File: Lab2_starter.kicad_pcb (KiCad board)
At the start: 4 copper layers, 123.2 x 64.6 mm, 78 parts, among them J1 973582101, J10 Conn_01x02, J11 Conn_01x02, J12 Conn_01x02, J13 Conn_01x02, J14 Conn_01x02, J15 Conn_01x02, J16 Conn_01x02, J2 973582100, J3 973582101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

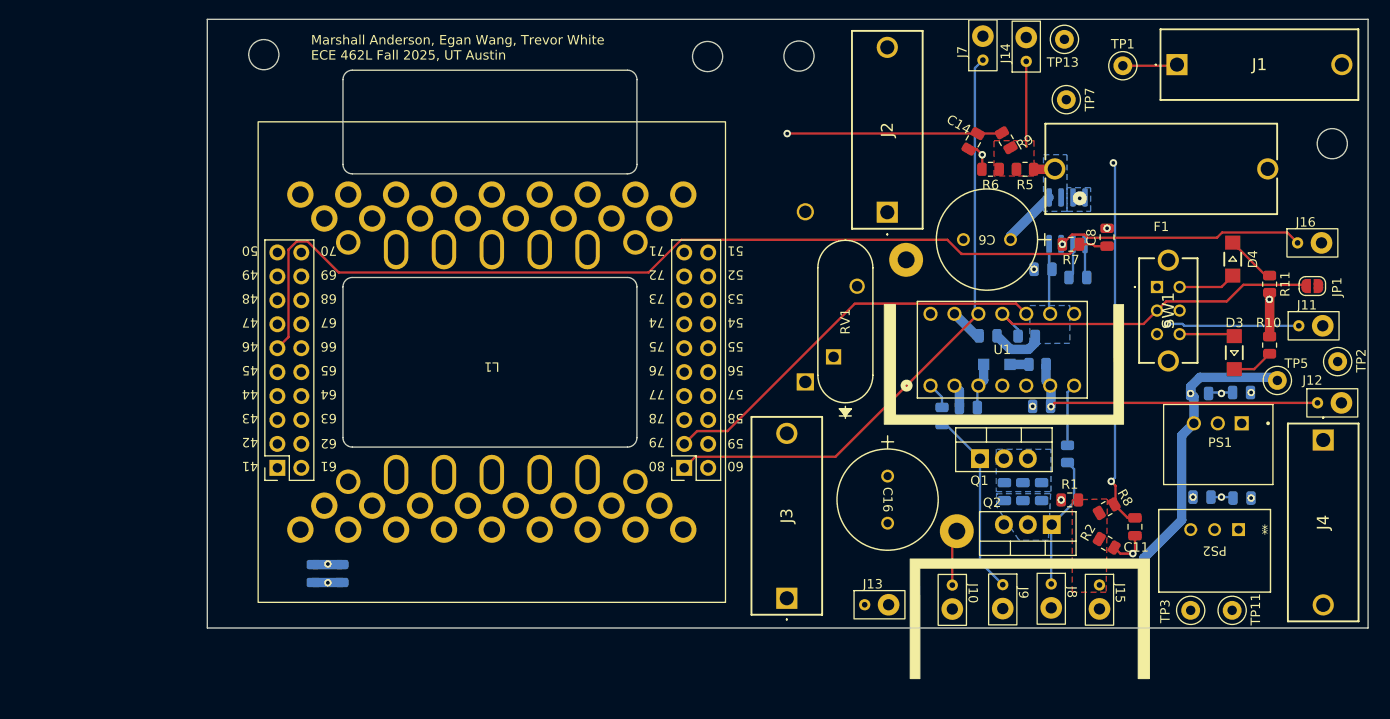
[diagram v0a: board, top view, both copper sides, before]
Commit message: Moved decoupling RC filters next to C2000 IO pins
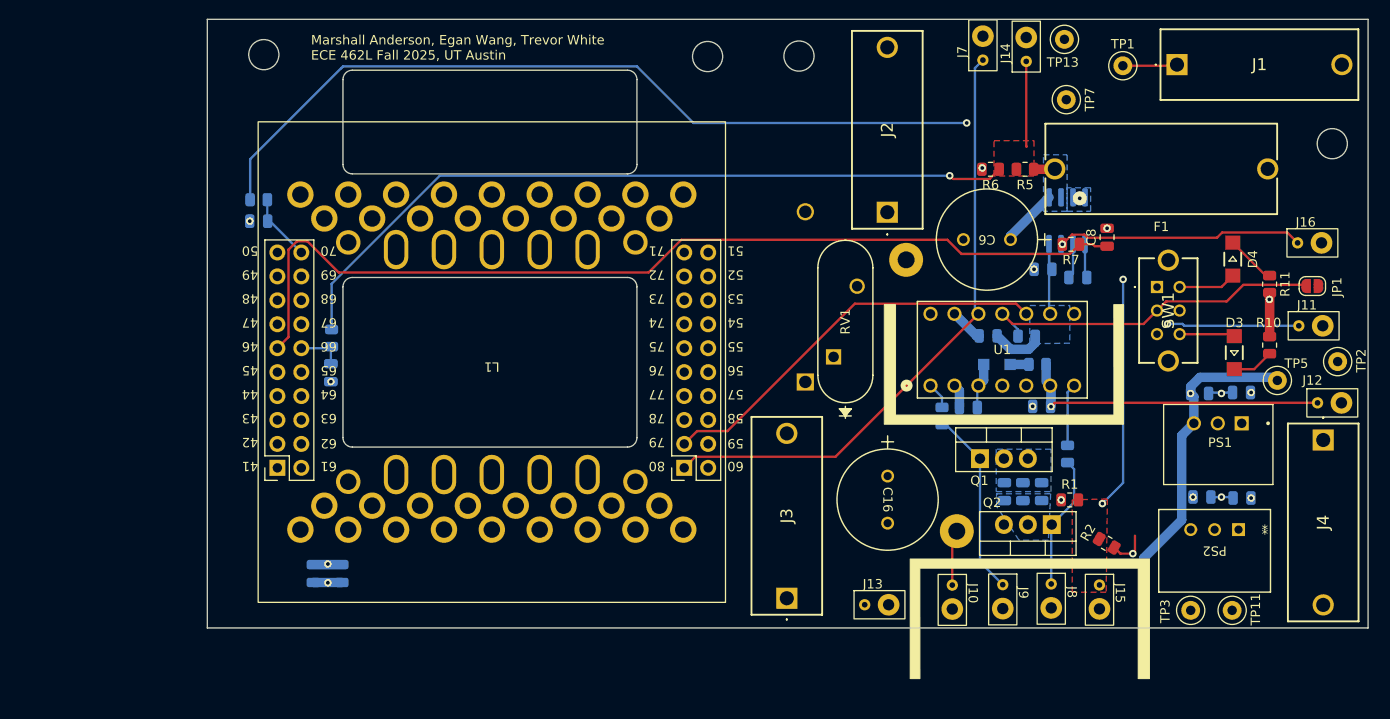
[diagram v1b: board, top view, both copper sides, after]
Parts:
- C11, C14, R8, R9: moved to B.Cu
- moved C11 98.5 mm to (36.5, 54.8), turned to 180 degrees
- moved R8 95.8 mm to (36.5, 52.5), turned to 180 degrees
- moved R9 74.6 mm to (44.2, 67.2), turned to 90 degrees
- moved C14 72.5 mm to (44.1, 70.9), turned to -90 degrees
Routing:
- net /ADCINA0: track 150.8 -> 7.24 mm, vias 2 -> 0
- net Vout_sens: track 0.00 -> 139.1 mm, vias 0 -> 3
- net Vin_sens: track 9.08 -> 90.1 mm, vias 0 -> 1
- net /ADCINA4: track 85.9 -> 5.12 mm, vias 1 -> 0
- net GND: track 26.6 -> 23.4 mm, vias 8 -> 10

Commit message: Add files via upload
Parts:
- C12, C15, C9: moved to F.Cu
- moved C15 3.95 mm to (115.6, 83.5)
- moved C9 3.95 mm to (119.5, 83.5)
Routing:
- added copper zone on F.Cu, net GND
- added copper zone on F.Cu, net Vout
- removed copper zone on B.Cu, net GND
- removed copper zone on B.Cu, net Vout

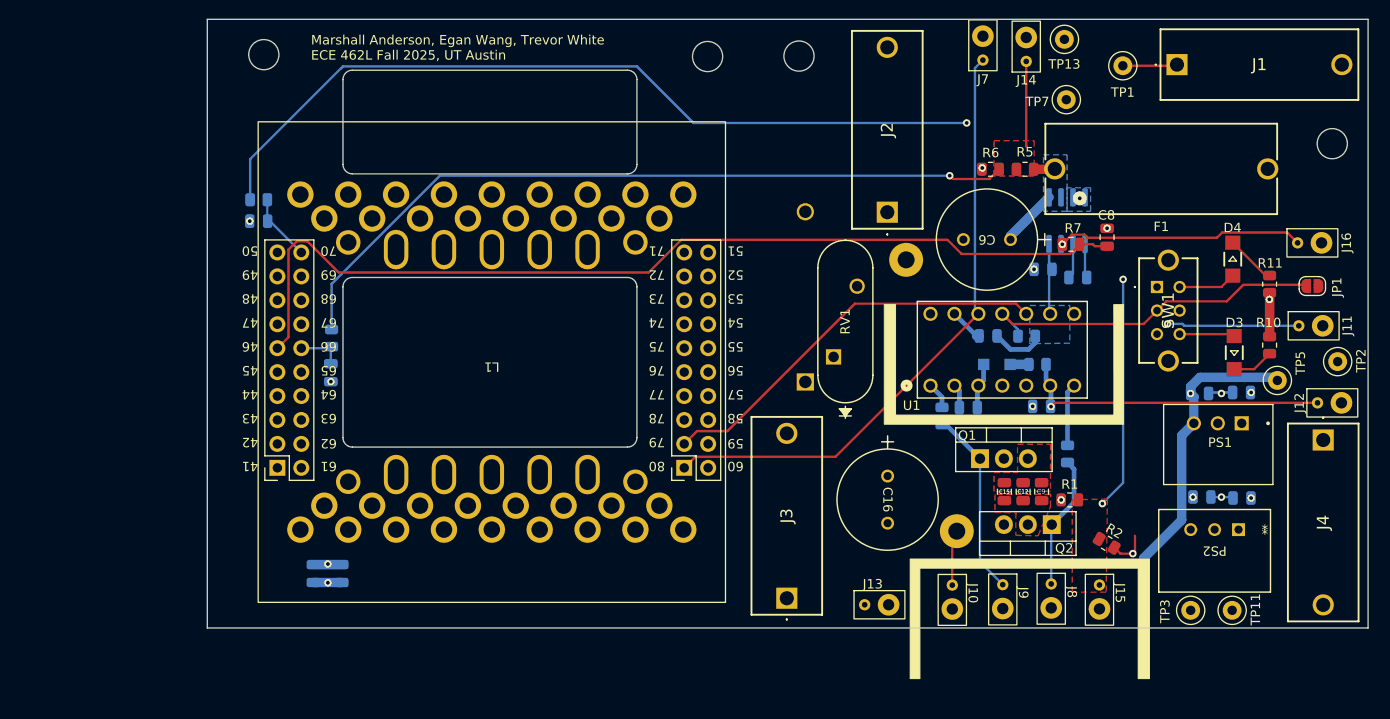
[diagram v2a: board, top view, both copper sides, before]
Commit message: updated PCB annulus, changed ADC traces
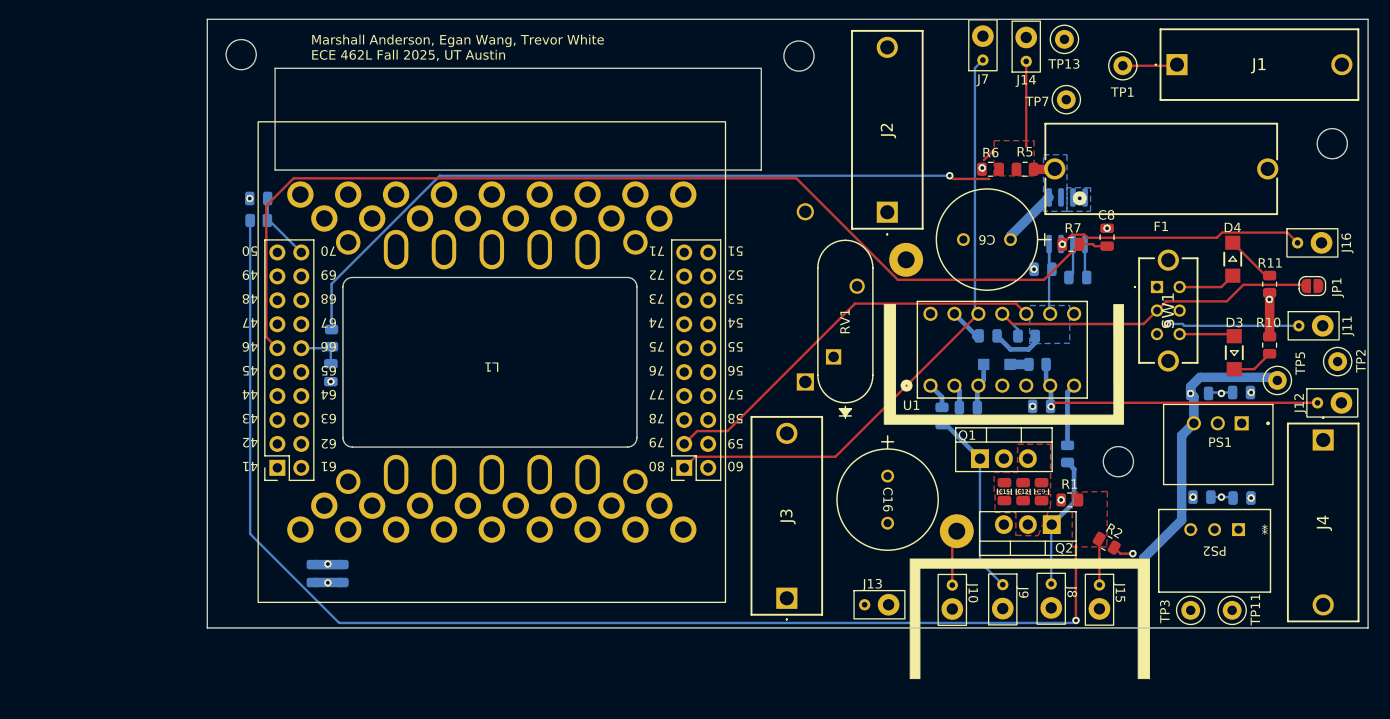
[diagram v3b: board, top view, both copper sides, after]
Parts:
- moved H4 61.2 mm to (127.7, 80.3)
- moved C11 2.40 mm to (36.5, 52.4)
- moved H3 2.40 mm to (34.6, 37.1)
- moved R8 2.20 mm to (36.5, 54.7)
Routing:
- net /ADCINA9: track 102.2 -> 112.2 mm
- net GND: track 23.4 -> 21.4 mm
- net Vout_sens: track 139.1 -> 137.8 mm, vias 3 -> 1
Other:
- outline, holes or cut-outs redrawn
- board text added: "{dblquote}High di/dt paths are inevitable in class society.{dblquote} -Mao Zedong"

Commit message: edited Mao quote spacing, further reduced board size
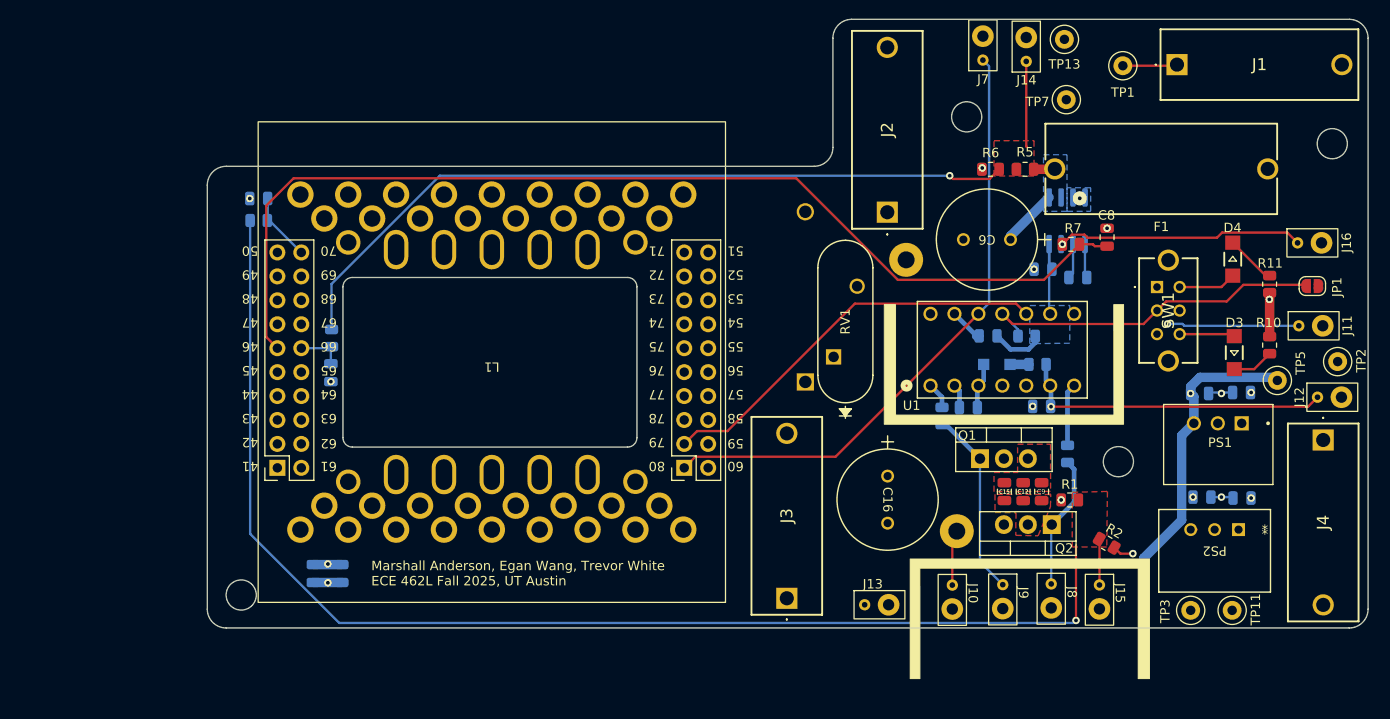
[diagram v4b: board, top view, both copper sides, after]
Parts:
- moved H1 82.3 mm to (34.6, 94.5)
- moved H3 77.3 mm to (111.6, 43.8)
- moved J12 0.60 mm to (150.1, 73.5)
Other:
- outline, holes or cut-outs redrawn
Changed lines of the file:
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@@
 	(footprint "MountingHole:MountingHole_3.2mm_M3"
 		(layer "F.Cu")
-		(at 93.8 37.3)
+		(at 34.6 94.5)
 		(descr "Mounting Hole 3.2mm, no annular, M3")
 		(tags "mounting hole 3.2mm no annular m3")
@@
 	(footprint "MountingHole:MountingHole_3.2mm_M3"
 		(layer "F.Cu")
-		(at 34.6 37.15)
+		(at 111.6 43.75)
 		(descr "Mounting Hole 3.2mm, no annular, M3")
 		(tags "mounting hole 3.2mm no annular m3")
@@
 	(footprint "ECE462L:TP"
 		(layer "F.Cu")
-		(at 150.105 74.108183)
+		(at 150.105 73.508183)
 		(property "Reference" "J12"
 			(at -3.185 0.001817 90)
@@
 		(layer "Edge.Cuts")
 	)
-	(gr_rect
-		(start 38.2 38.6)
-		(end 89.8 49.4)
+	(gr_line
+		(start 97.4 47)
+		(end 97.4 35.4)
 		(stroke
 			(width 0.1)
 			(type default)
 		)
-		(fill no)
 		(layer "Edge.Cuts")
 	)
-	(gr_rect
-		(start 31 33.4)
-		(end 154.2 98)
+	(gr_arc
+		(start 97.4 47)
+		(mid 96.814214 48.414214)
+		(end 95.4 49)
+		(stroke
+			(width 0.1)
+			(type default)
+		)
+		(layer "Edge.Cuts")
+	)
+	(gr_line
+		(start 152.2 98)
+		(end 33 98)
+		(stroke
+			(width 0.1)
+			(type default)
+		)
+		(layer "Edge.Cuts")
+	)
+	(gr_arc
+		(start 152.2 33.4)
+		(mid 153.614214 33.985786)
+		(end 154.2 35.4)
+		(stroke
+			(width 0.1)
+			(type default)
+		)
+		(layer "Edge.Cuts")
+	)
+	(gr_arc
+		(start 33 98)
+		(mid 31.585786 97.414214)
+		(end 31 96)
 		(stroke
 			(width 0.1)
 			(type default)
 		)
-		(fill no)
 		(layer "Edge.Cuts")
 	)
@@
 		(layer "Edge.Cuts")
 	)
+	(gr_arc
+		(start 31 51)
+		(mid 31.585786 49.585786)
+		(end 33 49)
+		(stroke
+			(width 0.1)
+			(type default)
+		)
+		(layer "Edge.Cuts")
+	)
+	(gr_arc
+		(start 97.4 35.4)
+		(mid 97.985786 33.985786)
+		(end 99.4 33.4)
+		(stroke
+			(width 0.1)
+			(type default)
+		)
+		(layer "Edge.Cuts")
+	)
+	(gr_line
+		(start 95.4 49)
+		(end 33 49)
+		(stroke
+			(width 0.1)
+			(type default)
+		)
+		(layer "Edge.Cuts")
+	)
+	(gr_line
+		(start 31 96)
+		(end 31 51)
+		(stroke
+			(width 0.1)
+			(type default)
+		)
+		(layer "Edge.Cuts")
+	)
+	(gr_arc
+		(start 154.2 96)
+		(mid 153.614214 97.414214)
+		(end 152.2 98)
+		(stroke
+			(width 0.1)
+			(type default)
+		)
+		(layer "Edge.Cuts")
+	)
 	(gr_line
 		(start 75.6 78.8)
@@
 	)
 	(gr_line
+		(start 99.4 33.4)
+		(end 152.2 33.4)
+		(stroke
+			(width 0.1)
+			(type default)
+		)
+		(layer "Edge.Cuts")
+	)
+	(gr_line
 		(start 76.6 61.8)
 		(end 76.6 77.8)
@@
 		(layer "Edge.Cuts")
 	)
+	(gr_line
+		(start 154.2 35.4)
+		(end 154.2 96)
+		(stroke
+			(width 0.1)
+			(type default)
+		)
+		(layer "Edge.Cuts")
+	)
 	(gr_rect
 		(start 30.95 33.4)
@@
 	)
 	(gr_text "Marshall Anderson, Egan Wang, Trevor White\nECE 462L Fall 2025, UT Austin"
-		(at 42 37.8 0)
+		(at 48.4 93.6 0)
 		(layer "F.SilkS")
 		(effects
@@
 		)
 	)
-	(gr_text "{dblquote}High di/dt paths are \ninevitable in class \nsociety.{dblquote} -Mao Zedong"
-		(at 108.151445 48.392694 0)
+	(gr_text "{dblquote}High di/dt \npaths are \ninevitable \nin class \nsociety.{dblquote} \n-Mao Zedong"
+		(at 107.593462 51.635218 0)
 		(layer "B.SilkS")
 		(effects
@@
 	)
 	(segment
-		(start 112.474 38.573304)
-		(end 112.474 64.291422)
+		(start 113.319882 37.727422)
+		(end 113.976 38.38354)
 		(width 0.25)
 		(layer "B.Cu")
@@
 	)
 	(segment
-		(start 113.319882 37.727422)
-		(end 112.474 38.573304)
+		(start 113.976 38.38354)
+		(end 113.976 63.521422)
 		(width 0.25)
 		(layer "B.Cu")
@@
 	)
 	(segment
-		(start 112.474 64.291422)
+		(start 113.976 63.521422)
 		(end 112.84 64.657422)
 		(width 0.25)
@@
 	)
 	(segment
-		(start 120.55 74.508183)
-		(end 120.95 74.108183)
+		(start 147.835 74.508183)
+		(end 120.55 74.508183)
 		(width 0.25)
 		(layer "F.Cu")
@@
 	)
 	(segment
-		(start 120.95 74.108183)
-		(end 148.835 74.108183)
+		(start 148.835 73.508183)
+		(end 147.835 74.508183)
 		(width 0.25)
 		(layer "F.Cu")
@@
 	)
 	(segment
-		(start 114.44375 47.31767)
-		(end 113.41775 48.34367)
+		(start 114.01775 50.34367)
+		(end 115.04375 49.31767)
 		(width 0.25)
 		(layer "F.Cu")

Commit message: shrunk driver loop, moved ADC sensing to be shorter - need to ask about hi dv/dt overlaying ground plane + low side decoupling cap
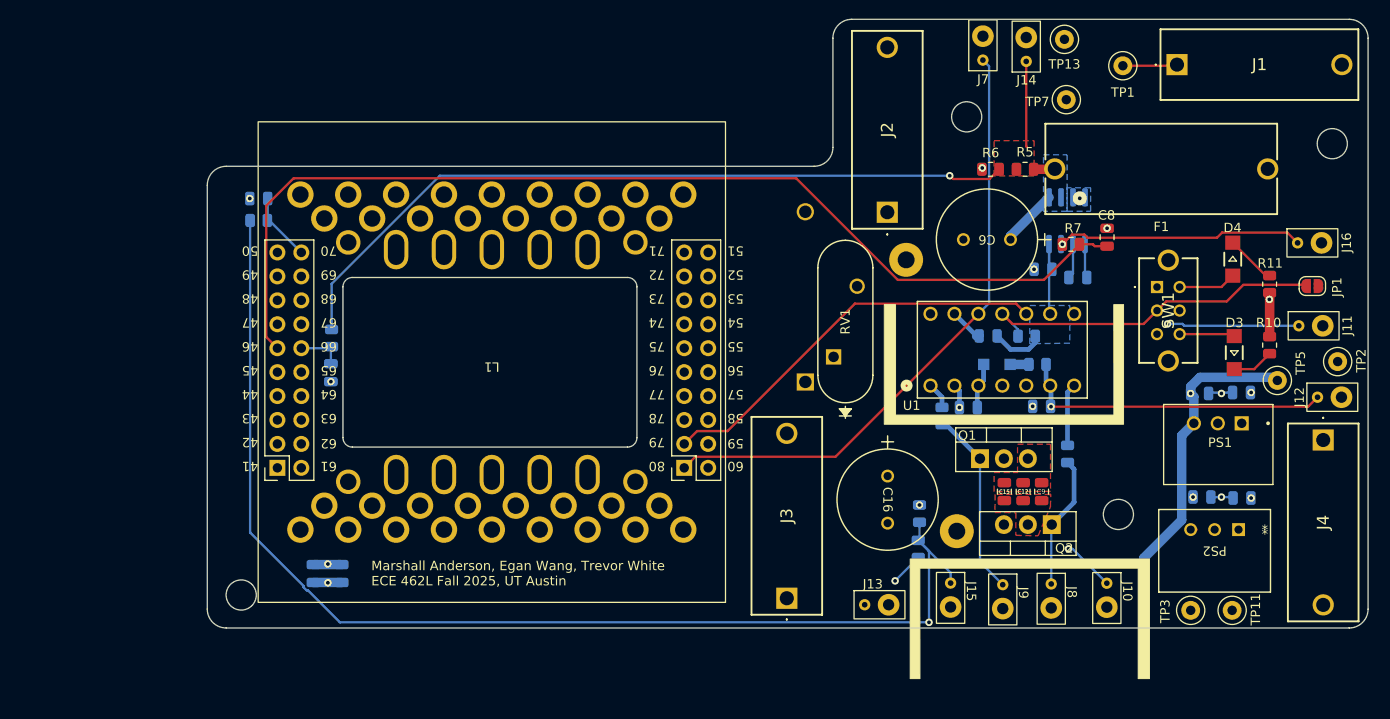
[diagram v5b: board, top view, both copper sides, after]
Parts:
- R1, R2: moved to B.Cu
- moved R2 20.0 mm to (106.5, 89.6), turned to -90 degrees
- moved J10 16.4 mm to (126.5, 94.5)
- moved R1 16.0 mm to (106.6, 85.9), turned to -90 degrees
- moved J15 15.8 mm to (109.9, 94.5)
- moved H4 5.60 mm to (127.7, 86.0)
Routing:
- net Vout_sens: track 137.8 -> 126.3 mm
- net GND: track 21.4 -> 22.3 mm, vias 10 -> 11
- net Vsw: track 6.17 -> 5.84 mm, vias 1 -> 2
- removed copper zone on F.Cu, net Vout_sens
